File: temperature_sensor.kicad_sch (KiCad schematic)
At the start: 18 parts, among them J1 USB_C_Receptacle_USB2.0_16P, U1 TMP37FT9Z, U2 AD589MH, U3 XIAO-SAMD21-SMD, U4 AD589MH, U5 TMP37FT9Z

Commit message: gonna change c to f conversion in digital instead of logically. this avoids the need to calculate current over Vout(-)'s voltage divider
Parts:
- removed J1: USB_C_Receptacle_USB2.0_16P, Connector_USB:USB_C_Receptacle_XKB_U262-16XN-4BVC11, symbol Connector:USB_C_Receptacle_USB2.0_16P
- removed R1, R2: 5.1k, symbol Device:R
- removed R3: 45.3k, symbol Device:R
- removed R4, R5: 10k, symbol Device:R
- removed R6: 182k, symbol Device:R
- removed RF_interceptor: 1u, symbol Device:C
- removed U1: TMP37FT9Z, TMP37FT9Z:TO254P508X660-3P, symbol TMP37FT9Z:TMP37FT9Z
- removed U2: AD589MH, AD589MH:TO127P557X381-2P, symbol AD589MH:AD589MH
- R10: footprint (none) -> Resistor_SMD:R_1210_3225Metric_Pad1.30x2.65mm_HandSolder
- R7, R8, R9: footprint (none) -> R_1210_3225Metric_Pad1.30x2.65mm_HandSolder
- RF_interceptor1: footprint (none) -> Capacitor_SMD:C_1210_3225Metric_Pad1.33x2.70mm_HandSolder
- U4: footprint AD589MH:TO127P557X381-2P -> 1_my_custom_library:AD589MH
- U5: footprint TMP37FT9Z:TO254P508X660-3P -> 1_my_custom_library:TMP37FT9Z
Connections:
- net GND: now also R10.1, R9.2, U3.20 (GND)
- net at U3.2 (PA4_A1_D1): now also R7.2, R8.1
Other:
- moved on the sheet: R10, R7, R8, R9, RF_interceptor1, U3

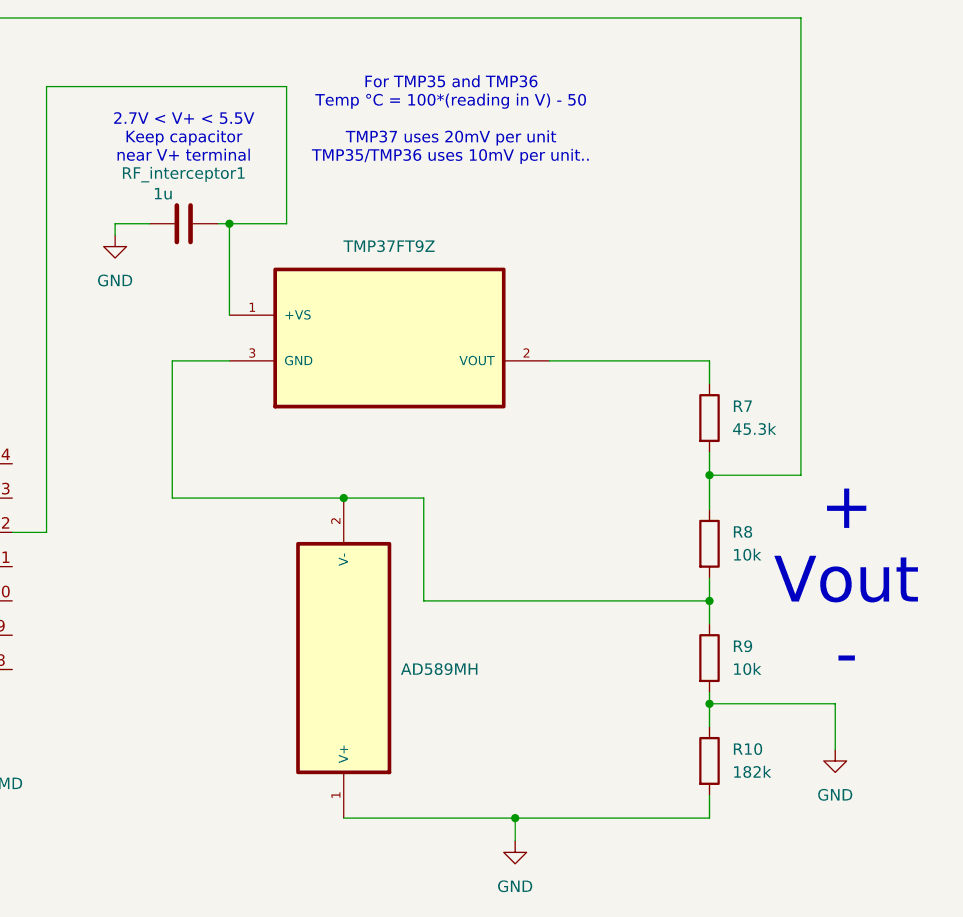
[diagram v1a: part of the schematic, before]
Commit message: lol this circuit got so much simpler
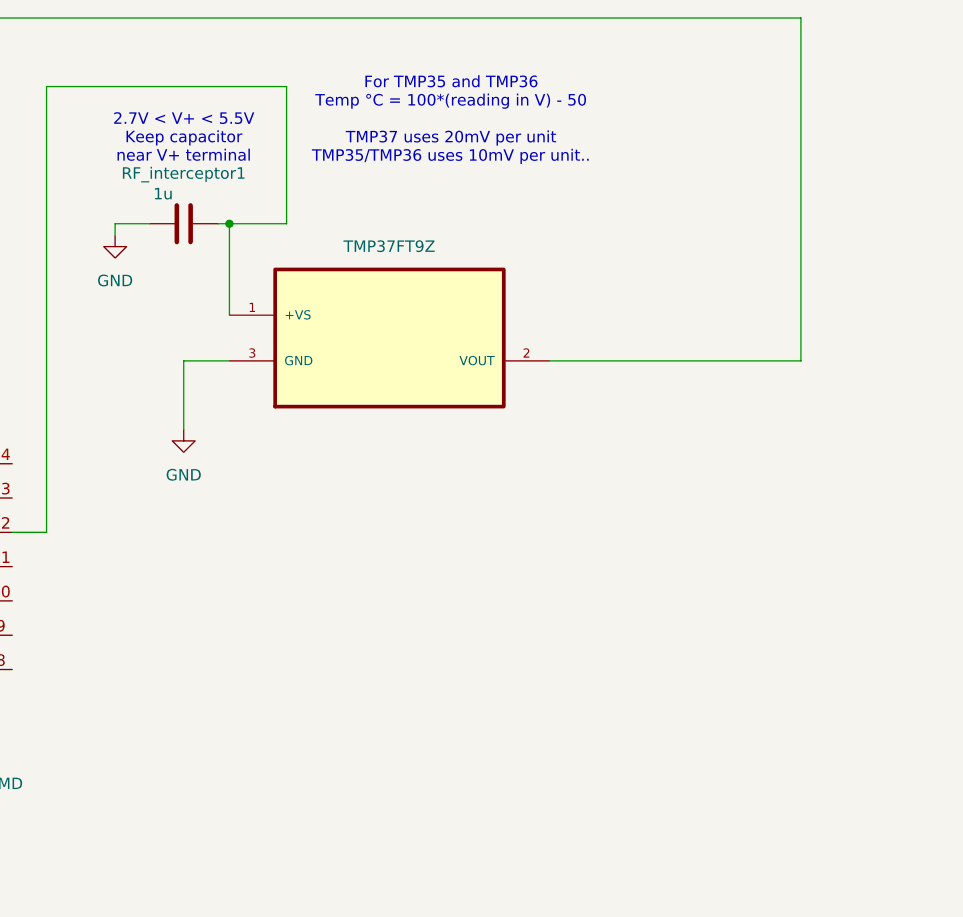
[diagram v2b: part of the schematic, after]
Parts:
- removed R10: 182k, Resistor_SMD:R_1210_3225Metric_Pad1.30x2.65mm_HandSolder, symbol Device:R
- removed R7: 45.3k, R_1210_3225Metric_Pad1.30x2.65mm_HandSolder, symbol Device:R
- removed R8, R9: 10k, R_1210_3225Metric_Pad1.30x2.65mm_HandSolder, symbol Device:R
- removed U4: AD589MH, 1_my_custom_library:AD589MH, symbol AD589MH:AD589MH
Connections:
- net GND: now also U5.3 (GND)
- net at U5.2 (VOUT): now also U3.2 (PA4_A1_D1)
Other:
- note removed: "+ Vout -"

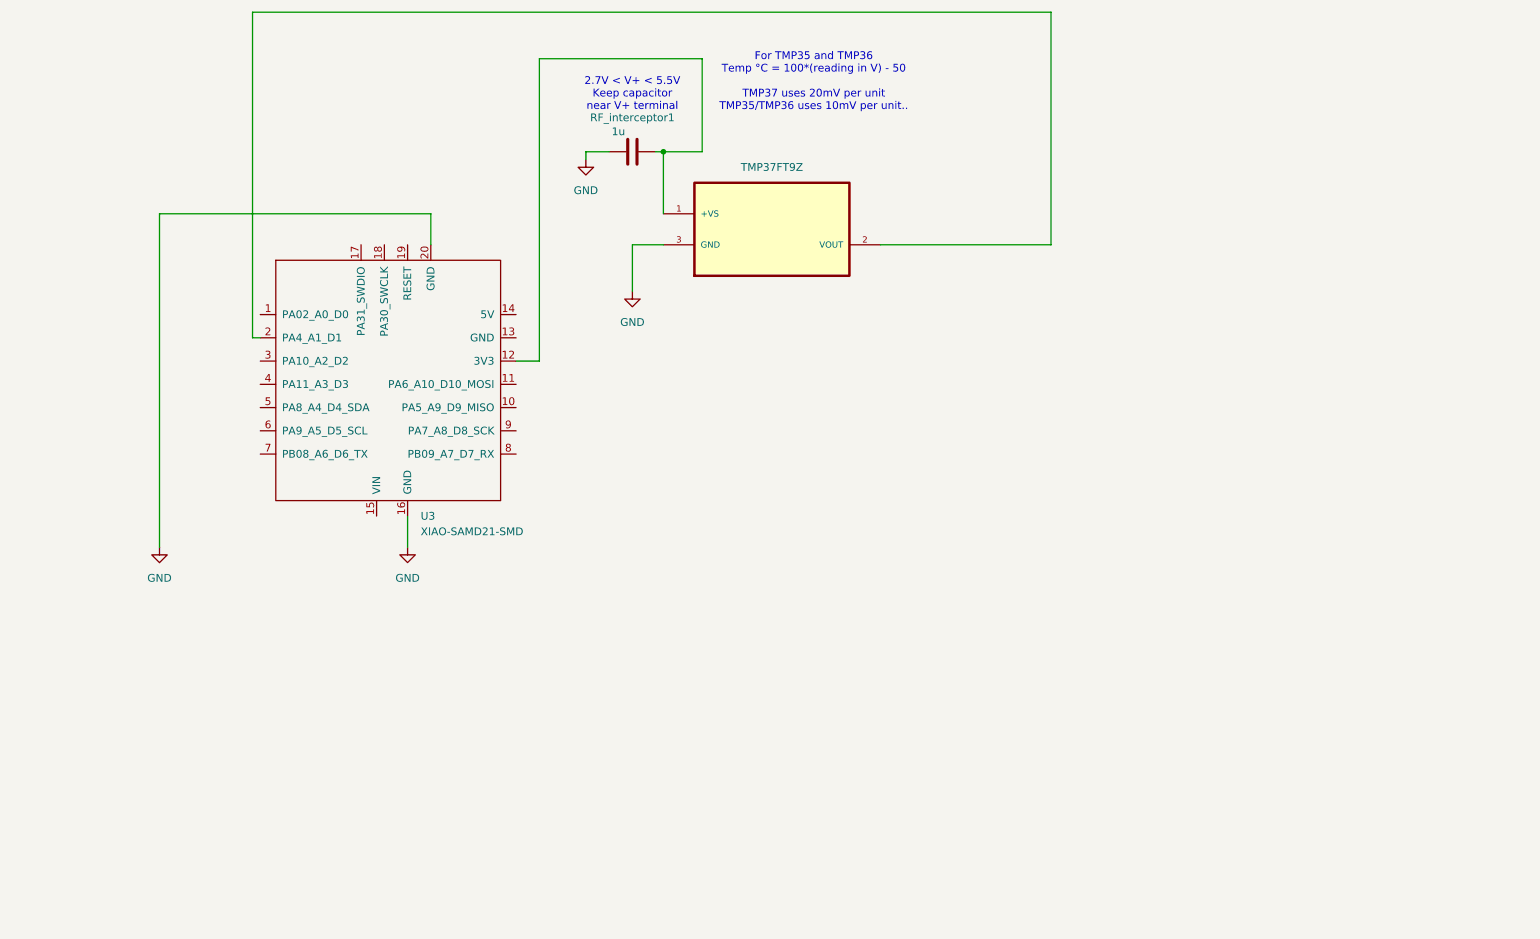
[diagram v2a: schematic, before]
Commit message: LCD screen. need to verify pins.  may need to swap to SPI if i cant hold ~CS1 low
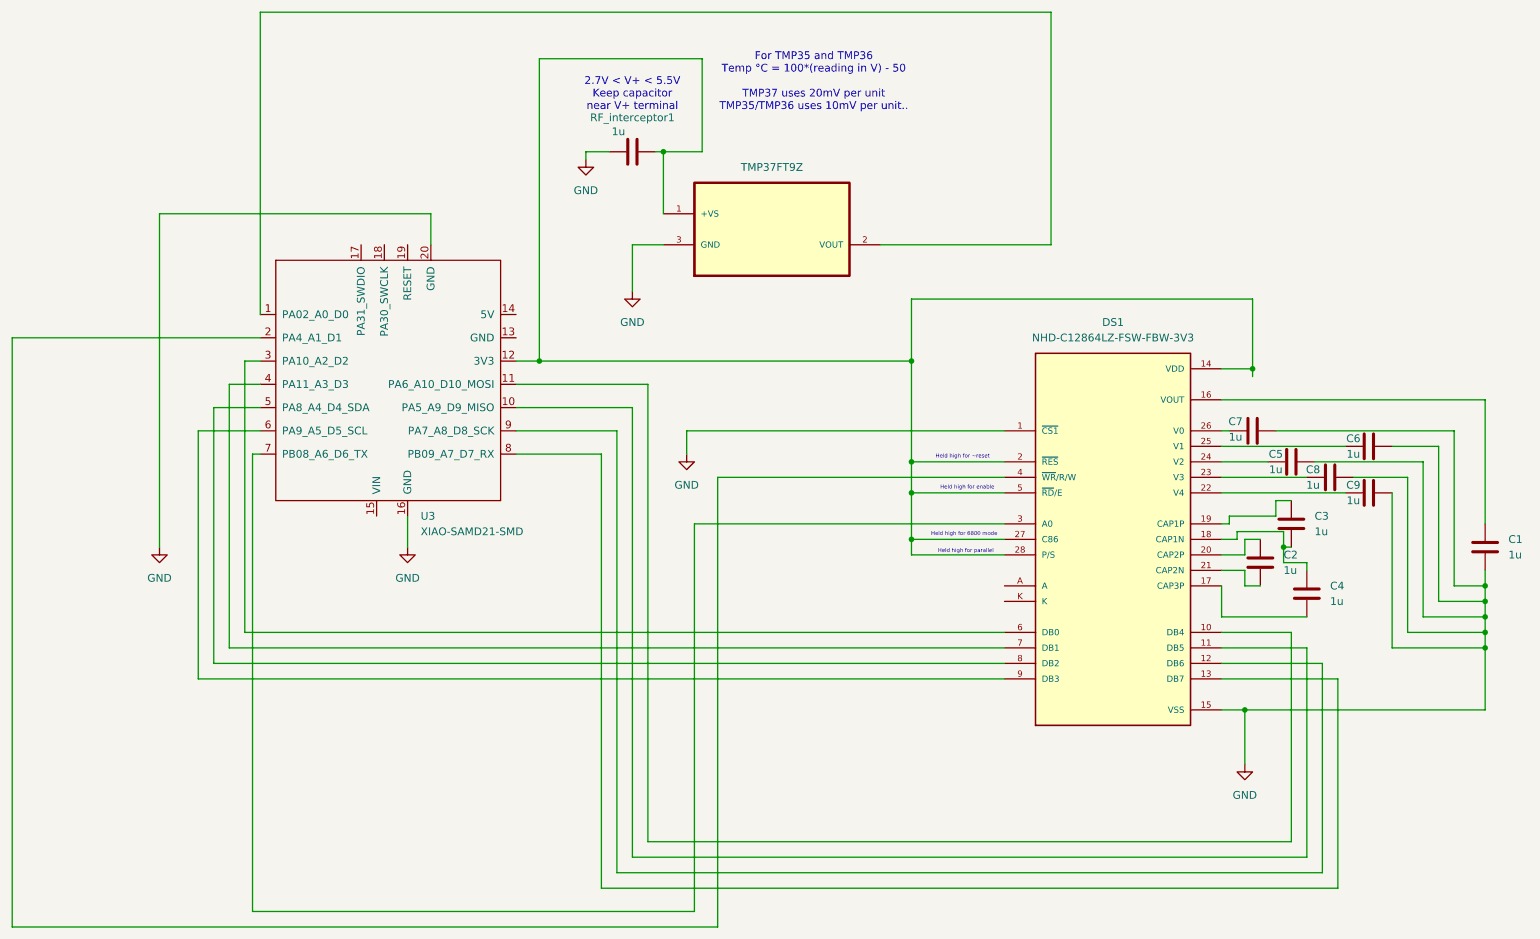
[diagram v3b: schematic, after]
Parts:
- added C1, C2, C3, C4, C5, C6, C7, C8, C9: 1u, symbol Device:C
- added DS1: NHD-C12864LZ-FSW-FBW-3V3, NHD-C12864LZ-FSW-FBW-3V3:LCD_NHD-C12864LZ-FSW-FBW-3V3, symbol NHD-C12864LZ-FSW-FBW-3V3:NHD-C12864LZ-FSW-FBW-3V3
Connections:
- net GND: now also C1.2, C5.2, C6.2, C7.2, C8.2, C9.2, DS1.1 (~{CS1}), DS1.15 (VSS)
- net at RF_interceptor1.2, U3.12 (3V3), U5.1 (+VS): now also DS1.14 (VDD), DS1.2 (~{RES}), DS1.27 (C86), DS1.28 (P/S), DS1.5 (~{RD}/E)
- net at U3.2 (PA4_A1_D1): now also DS1.4 (~{WR}/R/W); no longer U5.2 (VOUT)
- net at U3.1 (PA02_A0_D0): now also U5.2 (VOUT)
- net at U3.10 (PA5_A9_D9_MISO): now also DS1.11 (DB5)
- net at U3.11 (PA6_A10_D10_MOSI): now also DS1.10 (DB4)
- net at U3.3 (PA10_A2_D2): now also DS1.6 (DB0)
- net at U3.4 (PA11_A3_D3): now also DS1.7 (DB1)
- net at U3.5 (PA8_A4_D4_SDA): now also DS1.8 (DB2)
- net at U3.6 (PA9_A5_D5_SCL): now also DS1.9 (DB3)
- net at U3.7 (PB08_A6_D6_TX): now also DS1.3 (A0)
- net at U3.8 (PB09_A7_D7_RX): now also DS1.13 (DB7)
- net at U3.9 (PA7_A8_D8_SCK): now also DS1.12 (DB6)
- new net: C9.1, DS1.22 (V4)
- new net: C7.1, DS1.26 (V0)
- new net: C2.1, DS1.20 (CAP2P)
- new net: C2.2, DS1.21 (CAP2N)
- new net: C1.1, DS1.16 (VOUT)
- new net: C4.2, DS1.17 (CAP3P)
- new net: C3.2, C4.1, DS1.18 (CAP1N)
- new net: C3.1, DS1.19 (CAP1P)
- new net: C8.1, DS1.23 (V3)
- new net: C5.1, DS1.24 (V2)
- new net: C6.1, DS1.25 (V1)
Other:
- note added: "Held high for 6800 mode"
- note added: "Held high for enable"
- note added: "Held high for parallel"
- note added: "Held high for ~reset"
